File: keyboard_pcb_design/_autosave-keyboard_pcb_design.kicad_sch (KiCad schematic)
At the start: 39 parts, among them J1 USB_C_Receptacle_USB2.0_14P, SW1 Switch, SW2 Switch, SW3 Switch, SW4 Switch, SW5 Switch, U1 SC09147, U2 NCP1117-3.3_SOT223, U3 MX25L3233FM2I-08Q, U4 SMF05CT1G, X1 ABM8-272-T3

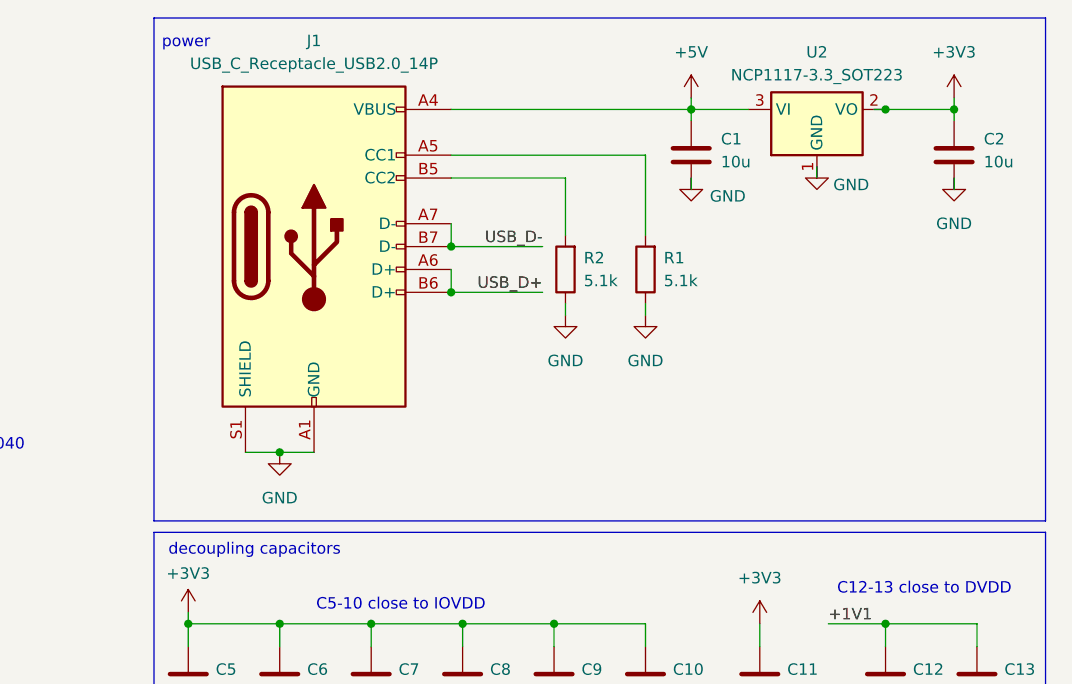
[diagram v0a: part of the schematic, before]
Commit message: update usbc and add footprints
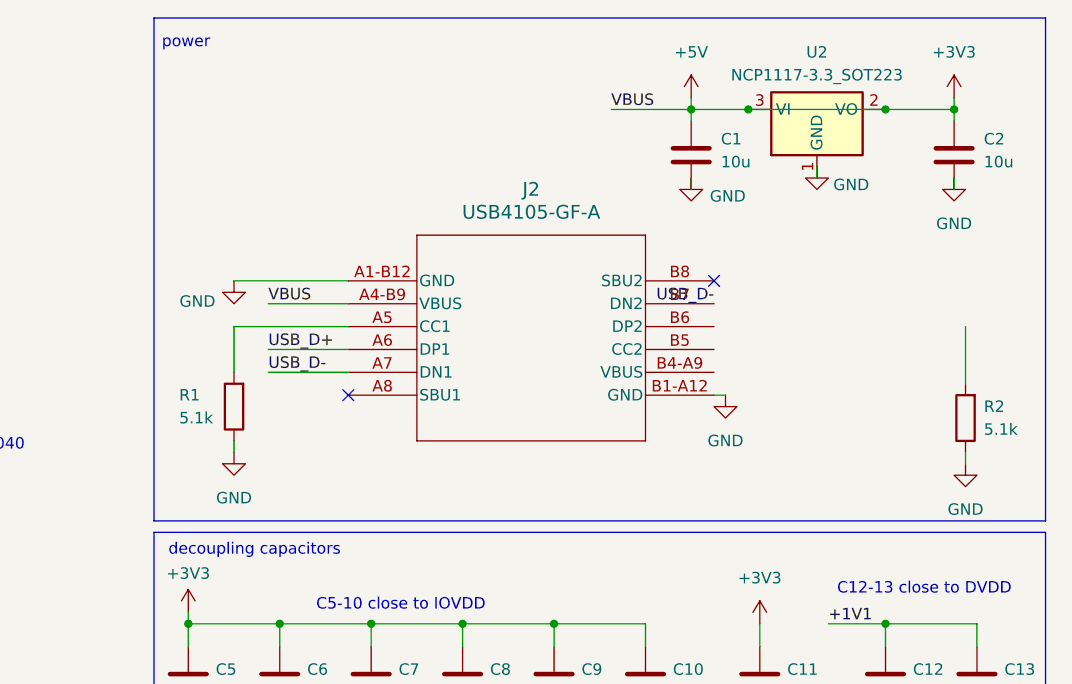
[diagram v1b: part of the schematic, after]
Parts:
- removed J1: USB_C_Receptacle_USB2.0_14P, symbol Connector:USB_C_Receptacle_USB2.0_14P
- added J2: USB4105-GF-A, symbol keyboard_library:USB4105-GF-A
- U4: footprint (none) -> keyboard_footprint:SOT65P210X110-6N
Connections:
- net +5V is gone; now on net +3V3: C1.1, U2.3 (VI), U4.4
- net +3V3: now also J2.A4-B9 (VBUS)
- net GND: now also J2.A1-B12 (GND), J2.B1-A12 (GND)
- net USB_D+: now also J2.A6 (DP1)
- net USB_D-: now also J2.A7 (DN1), J2.B7 (DN2)
- net at R1.2: now also J2.A5 (CC1)
- no-connect marks 1 -> 3
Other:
- moved on the sheet: R1, R2
